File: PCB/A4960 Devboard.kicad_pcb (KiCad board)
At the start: 2 copper layers, 43.4 x 48.8 mm, 58 parts, among them IC1 ATMEGA8-AI, P1 CONN_02X03, P2 CONN_01X02, P3 CONN_01X03, P4 CONN_01X03, Q1 Q_NMOS_GDS_old, Q2 Q_NMOS_GDS_old, Q3 Q_NMOS_GDS_old, Q4 Q_NMOS_GDS_old, Q5 Q_NMOS_GDS_old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

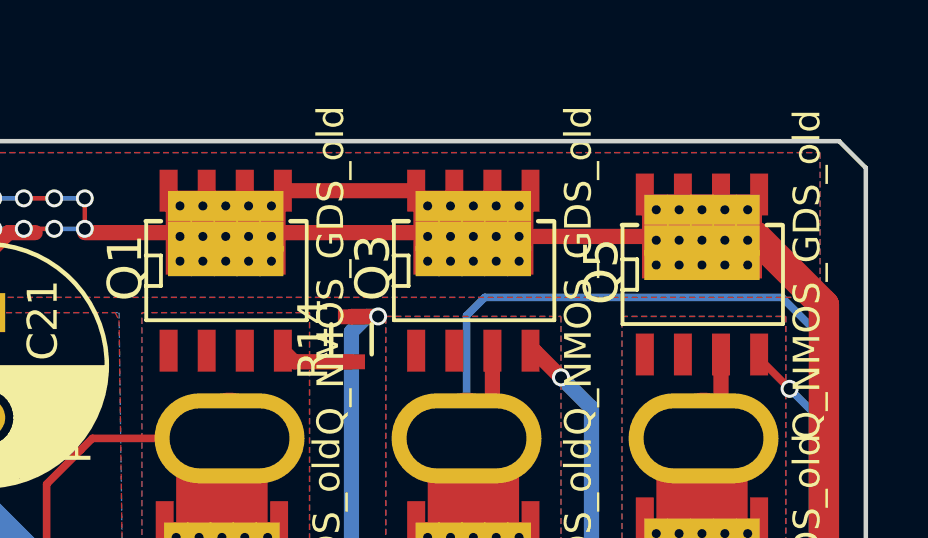
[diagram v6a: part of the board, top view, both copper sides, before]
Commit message: Lötstopplack auf unterseite teilweise entfernt
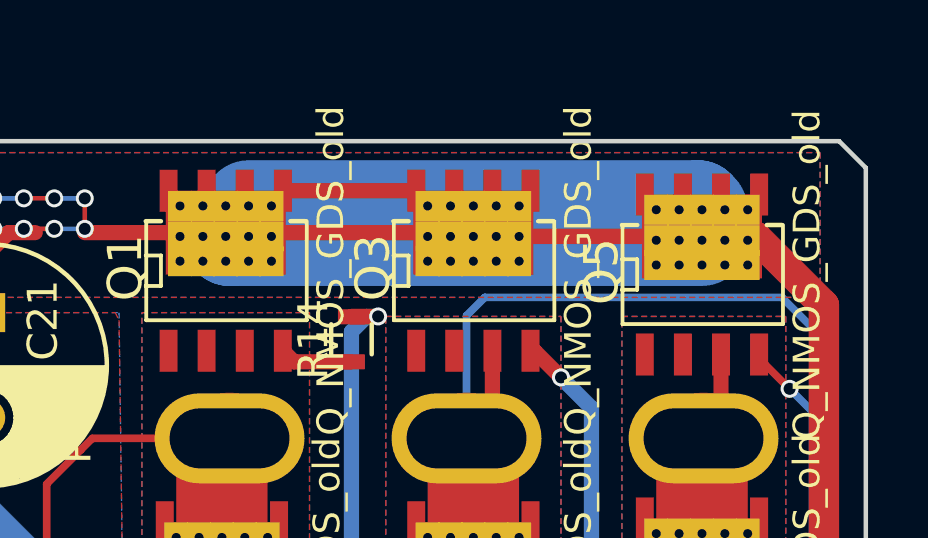
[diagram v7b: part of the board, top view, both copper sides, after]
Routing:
- net VPP: track 136.0 -> 174.6 mm
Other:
- rule pad_to_mask_clearance: 0.2 -> 0.1
- board text added: "(C) Philipp Hörauf"
- board text added: "Sven Schneider"
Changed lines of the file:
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@@
     (links 256)
     (no_connects 0)
-    (area 190.1452 63.3932 235.279001 117.354133)
+    (area 189.033674 63.3932 238.967846 117.354133)
     (thickness 1.6)
-    (drawings 8)
-    (tracks 854)
+    (drawings 72)
+    (tracks 859)
     (zones 0)
     (modules 58)
@@
     (0 F.Cu signal hide)
     (31 B.Cu signal)
-    (32 B.Adhes user hide)
-    (33 F.Adhes user hide)
-    (34 B.Paste user hide)
-    (35 F.Paste user hide)
+    (32 B.Adhes user)
+    (33 F.Adhes user)
+    (34 B.Paste user)
+    (35 F.Paste user)
     (36 B.SilkS user)
     (37 F.SilkS user)
-    (38 B.Mask user hide)
-    (39 F.Mask user hide)
+    (38 B.Mask user)
+    (39 F.Mask user)
     (40 Dwgs.User user hide)
     (41 Cmts.User user hide)
@@
   )
   (setup
-    (last_trace_width 0.508)
+    (last_trace_width 3.048)
     (user_trace_width 0.1524)
     (user_trace_width 0.254)
@@
     (zone_45_only no)
     (trace_min 0.1524)
-    (segment_width 0.2)
+    (segment_width 0.5)
     (edge_width 0.15)
     (via_size 0.6)
@@
     (pad_size 1 3.2)
     (pad_drill 0)
-    (pad_to_mask_clearance 0.2)
+    (pad_to_mask_clearance 0.1)
     (aux_axis_origin 0 0)
     (visible_elements FFFEFF7F)
@@
     (descr SO8_power_pak)
     (tags SMD_power_pak)
-    (zone_connect 0)
+    (zone_connect 2)
     (attr smd)
     (fp_text reference Q3 (at -3.35026 -0.09906 90) (layer F.SilkS)
@@
     (pad 1 thru_hole circle (at 0 0) (size 3 3) (drill 3) (layers))
   )
+  (gr_line (start 219.5 102.5) (end 224 98) (angle 90) (layer B.Mask) (width 0.5))
+  (gr_line (start 214 98.5) (end 217.5 102) (angle 90) (layer B.Mask) (width 0.5))
+  (gr_line (start 214 92) (end 214 98.5) (angle 90) (layer B.Mask) (width 0.5))
+  (gr_line (start 212 90) (end 214 92) (angle 90) (layer B.Mask) (width 0.5))
+  (gr_line (start 209 90) (end 212 90) (angle 90) (layer B.Mask) (width 0.5))
+  (gr_line (start 206 87) (end 209 90) (angle 90) (layer B.Mask) (width 0.5))
+  (gr_line (start 206 85.5) (end 206 87) (angle 90) (layer B.Mask) (width 0.5))
+  (gr_line (start 206.5 87) (end 206.5 85.5) (angle 90) (layer B.Mask) (width 0.5))
+  (gr_line (start 209 89.5) (end 206.5 87) (angle 90) (layer B.Mask) (width 0.5))
+  (gr_line (start 212 89.5) (end 209 89.5) (angle 90) (layer B.Mask) (width 0.5))
+  (gr_line (start 214.5 92) (end 212 89.5) (angle 90) (layer B.Mask) (width 0.5))
+  (gr_line (start 214.5 98.5) (end 214.5 92) (angle 90) (layer B.Mask) (width 0.5))
+  (gr_line (start 215 99) (end 214.5 98.5) (angle 90) (layer B.Mask) (width 0.5))
+  (gr_line (start 218 102) (end 215 99) (angle 90) (layer B.Mask) (width 0.5))
+  (gr_line (start 218.5 102) (end 218 102) (angle 90) (layer B.Mask) (width 0.5))
+  (gr_line (start 219 102.5) (end 218.5 102) (angle 90) (layer B.Mask) (width 0.5))
+  (gr_line (start 224.5 97) (end 219 102.5) (angle 90) (layer B.Mask) (width 0.5))
+  (gr_text "Sven Schneider\n" (at 194.5 92 270) (layer B.SilkS)
+    (effects (font (size 1.5 1.5) (thickness 0.3)) (justify mirror))
+  )
+  (gr_text "(C) Philipp Hörauf\n" (at 197 94.5 270) (layer B.SilkS)
+    (effects (font (size 1.5 1.5) (thickness 0.3)) (justify mirror))
+  )
+  (gr_line (start 227.5 69) (end 228 69) (angle 90) (layer B.Mask) (width 0.5))
+  (gr_line (start 226 70.5) (end 227.5 69) (angle 90) (layer B.Mask) (width 0.5))
+  (gr_line (start 224.5 69) (end 226 70.5) (angle 90) (layer B.Mask) (width 0.5))
+  (gr_line (start 224 69) (end 224.5 69) (angle 90) (layer B.Mask) (width 0.5))
+  (gr_line (start 219.5 70.5) (end 220 70) (angle 90) (layer B.Mask) (width 0.5))
+  (gr_line (start 217.5 68.5) (end 219.5 70.5) (angle 90) (layer B.Mask) (width 0.5))
+  (gr_line (start 216 70) (end 217.5 68.5) (angle 90) (layer B.Mask) (width 0.5))
+  (gr_line (start 211.5 70) (end 212 70) (angle 90) (layer B.Mask) (width 0.5))
+  (gr_line (start 210 68.5) (end 211.5 70) (angle 90) (layer B.Mask) (width 0.5))
+  (gr_line (start 208 70.5) (end 210 68.5) (angle 90) (layer B.Mask) (width 0.5))
+  (gr_line (start 206 68.5) (end 208 70.5) (angle 90) (layer B.Mask) (width 0.5))
+  (gr_line (start 204 70.5) (end 206 68.5) (angle 90) (layer B.Mask) (width 0.5))
+  (gr_line (start 202 68.5) (end 204 70.5) (angle 90) (layer B.Mask) (width 0.5))
+  (gr_line (start 200 70.5) (end 202 68.5) (angle 90) (layer B.Mask) (width 0.5))
+  (gr_line (start 201.5 80) (end 199 80) (angle 90) (layer B.Mask) (width 0.5))
+  (gr_line (start 202.5 81) (end 201.5 80) (angle 90) (layer B.Mask) (width 0.5))
+  (gr_line (start 202.5 84) (end 202.5 81) (angle 90) (layer B.Mask) (width 0.5))
+  (gr_line (start 206.5 80.5) (end 206.5 84) (angle 90) (layer B.Mask) (width 0.5))
+  (gr_line (start 202.5 76.5) (end 206.5 80.5) (angle 90) (layer B.Mask) (width 0.5))
+  (gr_line (start 199.5 76.5) (end 202.5 76.5) (angle 90) (layer B.Mask) (width 0.5))
+  (gr_line (start 202 78.5) (end 199.5 78.5) (angle 90) (layer B.Mask) (width 0.5))
+  (gr_line (start 204.5 81) (end 202 78.5) (angle 90) (layer B.Mask) (width 0.5))
+  (gr_line (start 204.5 84) (end 204.5 81) (angle 90) (layer B.Mask) (width 0.5))
+  (gr_line (start 212 84.5) (end 224 84.5) (angle 90) (layer B.Mask) (width 0.5))
+  (gr_line (start 210 82.5) (end 212 84.5) (angle 90) (layer B.Mask) (width 0.5))
+  (gr_line (start 211.5 86) (end 210 84.5) (angle 90) (layer B.Mask) (width 0.5))
+  (gr_line (start 224.5 86) (end 211.5 86) (angle 90) (layer B.Mask) (width 0.5))
+  (gr_line (start 226 84.5) (end 224.5 86) (angle 90) (layer B.Mask) (width 0.5))
+  (gr_line (start 227.5 86) (end 226 84.5) (angle 90) (layer B.Mask) (width 0.5))
+  (gr_line (start 231 86) (end 227.5 86) (angle 90) (layer B.Mask) (width 0.5))
+  (gr_line (start 227.5 68.5) (end 228 68.5) (angle 90) (layer B.Mask) (width 0.5))
+  (gr_line (start 226 70) (end 227.5 68.5) (angle 90) (layer B.Mask) (width 0.5))
+  (gr_line (start 224.5 68.5) (end 226 70) (angle 90) (layer B.Mask) (width 0.5))
+  (gr_line (start 224 68.5) (end 224.5 68.5) (angle 90) (layer B.Mask) (width 0.5))
+  (gr_line (start 219.5 70) (end 220.5 69) (angle 90) (layer B.Mask) (width 0.5))
+  (gr_line (start 217.5 68) (end 219.5 70) (angle 90) (layer B.Mask) (width 0.5))
+  (gr_line (start 216 69.5) (end 217.5 68) (angle 90) (layer B.Mask) (width 0.5))
+  (gr_line (start 215.5 69.5) (end 216 69.5) (angle 90) (layer B.Mask) (width 0.5))
+  (gr_line (start 211.5 69.5) (end 212 69.5) (angle 90) (layer B.Mask) (width 0.5))
+  (gr_line (start 210 68) (end 211.5 69.5) (angle 90) (layer B.Mask) (width 0.5))
+  (gr_line (start 208 70) (end 210 68) (angle 90) (layer B.Mask) (width 0.5))
+  (gr_line (start 206 68) (end 208 70) (angle 90) (layer B.Mask) (width 0.5))
+  (gr_line (start 204 70) (end 206 68) (angle 90) (layer B.Mask) (width 0.5))
+  (gr_line (start 202 68) (end 204 70) (angle 90) (layer B.Mask) (width 0.5))
+  (gr_line (start 200 70) (end 202 68) (angle 90) (layer B.Mask) (width 0.5))
   (gr_line (start 191.77 66.167) (end 234.315 66.167) (angle 90) (layer Edge.Cuts) (width 0.15))
   (gr_line (start 191.77 113.157) (end 191.77 66.167) (angle 90) (layer Edge.Cuts) (width 0.15))
@@
   (segment (start 212.229 96.012) (end 212.229 97.663) (width 0.1524) (layer F.Cu) (net 6))
   (segment (start 211.062 96.012) (end 212.229 96.012) (width 0.1524) (layer F.Cu) (net 6))
+  (segment (start 214.63 68.326) (end 229.616 68.326) (width 3.048) (layer B.Cu) (net 7) (status C00000))
+  (segment (start 229.616 68.326) (end 229.743 68.453) (width 3.048) (layer B.Cu) (net 7) (status C00000))
+  (segment (start 229.743 69.469) (end 213.995 69.469) (width 3.048) (layer B.Cu) (net 7) (status C00000))
+  (segment (start 213.995 69.469) (end 213.868 69.342) (width 3.048) (layer B.Cu) (net 7) (status C00000))
+  (segment (start 222.123 69.342) (end 214.63 69.342) (width 0.1524) (layer B.Cu) (net 7) (status C00000))
   (via (at 209.169 69.088) (size 0.6) (drill 0.4) (layers F.Cu B.Cu) (net 7))
   (segment (start 207.137 69.088) (end 208.153 69.088) (width 0.1524) (layer F.Cu) (net 7))

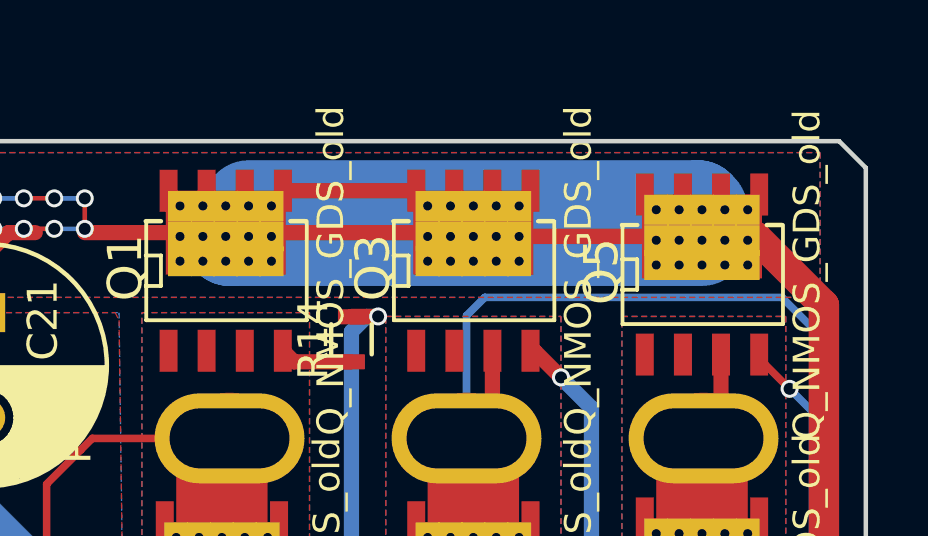
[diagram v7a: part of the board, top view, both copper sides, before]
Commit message: Q3 war nicht richtig angeschlossen...
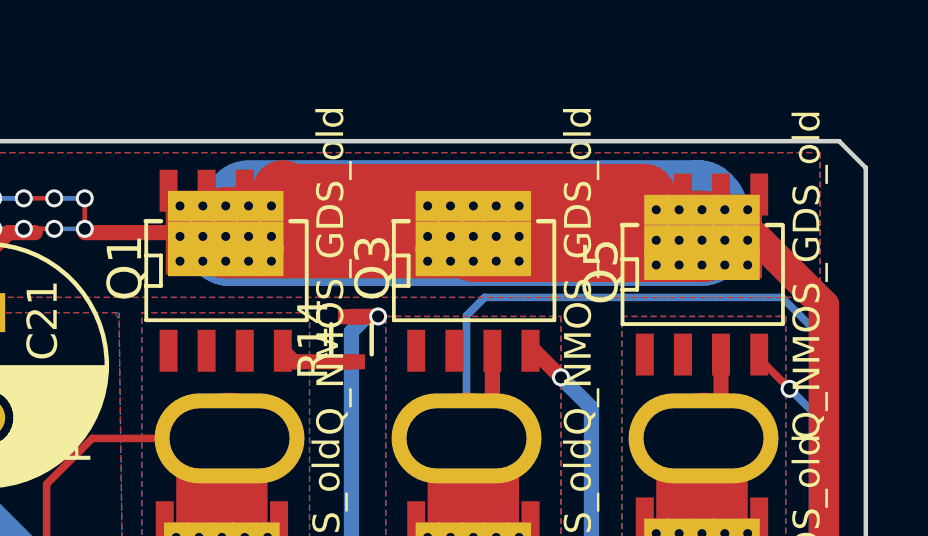
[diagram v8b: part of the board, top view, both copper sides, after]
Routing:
- net VPP: track 174.6 -> 195.1 mm
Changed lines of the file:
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@@
     (thickness 1.6)
     (drawings 72)
-    (tracks 859)
+    (tracks 863)
     (zones 0)
     (modules 58)
@@
   (page A4)
   (layers
-    (0 F.Cu signal hide)
-    (31 B.Cu signal)
+    (0 F.Cu signal)
+    (31 B.Cu signal hide)
     (32 B.Adhes user)
     (33 F.Adhes user)
@@
   )
   (setup
-    (last_trace_width 3.048)
+    (last_trace_width 0.1524)
     (user_trace_width 0.1524)
     (user_trace_width 0.254)
@@
   (segment (start 212.229 96.012) (end 212.229 97.663) (width 0.1524) (layer F.Cu) (net 6))
   (segment (start 211.062 96.012) (end 212.229 96.012) (width 0.1524) (layer F.Cu) (net 6))
-  (segment (start 214.63 68.326) (end 229.616 68.326) (width 3.048) (layer B.Cu) (net 7) (status C00000))
-  (segment (start 229.616 68.326) (end 229.743 68.453) (width 3.048) (layer B.Cu) (net 7) (status C00000))
-  (segment (start 229.743 69.469) (end 213.995 69.469) (width 3.048) (layer B.Cu) (net 7) (status C00000))
-  (segment (start 213.995 69.469) (end 213.868 69.342) (width 3.048) (layer B.Cu) (net 7) (status C00000))
-  (segment (start 222.123 69.342) (end 214.63 69.342) (width 0.1524) (layer B.Cu) (net 7) (status C00000))
+  (segment (start 227.838 67.945) (end 215.9 67.945) (width 2.032) (layer F.Cu) (net 7))
+  (segment (start 215.9 67.945) (end 215.773 67.818) (width 2.032) (layer F.Cu) (net 7))
+  (segment (start 229.743 69.342) (end 222.25 69.342) (width 3.048) (layer F.Cu) (net 7))
+  (segment (start 222.25 69.342) (end 222.123 69.215) (width 3.048) (layer F.Cu) (net 7))
+  (segment (start 222.123 69.215) (end 213.868 69.215) (width 3.048) (layer F.Cu) (net 7))
+  (segment (start 214.63 68.326) (end 229.616 68.326) (width 3.048) (layer B.Cu) (net 7))
+  (segment (start 229.616 68.326) (end 229.743 68.453) (width 3.048) (layer B.Cu) (net 7))
+  (segment (start 229.743 69.469) (end 213.995 69.469) (width 3.048) (layer B.Cu) (net 7))
+  (segment (start 213.995 69.469) (end 213.868 69.342) (width 3.048) (layer B.Cu) (net 7))
+  (segment (start 222.123 69.342) (end 214.63 69.342) (width 0.1524) (layer B.Cu) (net 7))
   (via (at 209.169 69.088) (size 0.6) (drill 0.4) (layers F.Cu B.Cu) (net 7))
   (segment (start 207.137 69.088) (end 208.153 69.088) (width 0.1524) (layer F.Cu) (net 7))
@@
   (segment (start 209.169 69.215) (end 222.123 69.215) (width 0.508) (layer F.Cu) (net 7))
   (segment (start 222.123 69.215) (end 222.25 69.342) (width 0.508) (layer F.Cu) (net 7))
-  (segment (start 222.25 69.342) (end 229.743 69.342) (width 0.508) (layer F.Cu) (net 7))
   (segment (start 205.867 71.882) (end 205.867 70.104) (width 0.508) (layer F.Cu) (net 7))
   (segment (start 205.359 69.596) (end 200.787 69.596) (width 0.508) (layer F.Cu) (net 7))
